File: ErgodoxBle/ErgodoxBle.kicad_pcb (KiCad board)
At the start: 2 copper layers, 182.8 x 158.9 mm, 120 parts, among them SW0:10 SW0:3, SW0:11 SW0:2, SW0:12 SW0:1, SW0:7 SW0:6, SW0:8 SW0:5, SW0:9 SW0:4, SW1:10 SW1:3, SW1:11 SW1:2, SW1:12 SW1:1, SW1:13 SW1:0, SW1:9 SW1:4, SW2:10 SW2:3, SW2:11 SW2:2, SW2:12 SW2:1, SW2:13 SW2:0, SW2:7 SW2:6, SW2:8 SW2:5, SW2:9 SW2:4, SW3:10 SW3:3, SW3:11 SW3:2, SW3:12 SW3:1, SW3:13 SW3:0, SW3:8 SW3:5, SW3:9 SW3:4, SW4:10 SW4:3, SW4:11 SW4:2, SW4:12 SW4:1, SW4:13 SW4:0, SW4:7 SW4:6, SW4:8 SW4:5, SW4:9 SW4:4, SW5:10 SW5:3, SW5:11 SW5:2, SW5:12 SW5:1, SW5:13 SW5:0, SW5:7 SW5:6, SW5:8 SW5:5, SW5:9 SW5:4

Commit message: schema and pcb pdf
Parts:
- removed the REF** at (172.9, 56.5)
- removed the REF** at (143.3, 76.1)
- removed the REF** at (67.8, 145.7)
- removed the REF** at (96.1, 157.6)
- removed the REF** at (158.3, 141.6)
- removed the REF** at (149.2, 145.2)
- removed the REF** at (142.6, 147.3)
- removed the REF** at (156.2, 126.8)
- removed the REF** at (154.9, 87.9)
- removed the REF** at (156.0, 105.3)
- removed the REF** at (156.3, 113.7)
- removed the REF** at (60.6, 176.1)
- removed the REF** at (91.8, 70.0)
- removed the REF** at (167.9, 110.0)
- removed the REF** at (138.9, 141.5)
- removed the REF** at (121.4, 84.8)
- removed the REF** at (121.4, 67.6)
- removed the REF** at (120.7, 124.0)
- removed the REF** at (123.4, 104.2)
- removed the REF** at (92.4, 88.5)
- removed the REF** at (103.5, 76.0)
- removed the REF** at (73.4, 164.6)
- removed the REF** at (177.3, 37.8)
- removed the REF** at (91.8, 108.3)
- removed the REF** at (168.9, 71.3)
- removed the REF** at (149.0, 49.6)
- removed the REF** at (139.6, 45.1)
- removed the REF** at (148.9, 68.7)
- added REF**: VIA-0.6mm, Keebio-Parts:VIA-0.6mm, F.Cu at (142.2, 38.5)
- added REF**: VIA-0.6mm, Keebio-Parts:VIA-0.6mm, F.Cu at (166.8, 129.4)
- added REF**: VIA-0.6mm, Keebio-Parts:VIA-0.6mm, F.Cu at (168.5, 109.1)
- added REF**: VIA-0.6mm, Keebio-Parts:VIA-0.6mm, F.Cu at (154.3, 86.6)
- added REF**: VIA-0.6mm, Keebio-Parts:VIA-0.6mm, F.Cu at (100.5, 123.8)
- added REF**: VIA-0.6mm, Keebio-Parts:VIA-0.6mm, F.Cu at (139.2, 122.6)
- added REF**: VIA-0.6mm, Keebio-Parts:VIA-0.6mm, F.Cu at (139.5, 104.1)
- added REF**: VIA-0.6mm, Keebio-Parts:VIA-0.6mm, F.Cu at (139.6, 90.9)
- added REF**: VIA-0.6mm, Keebio-Parts:VIA-0.6mm, F.Cu at (168.2, 71.8)
- added REF**: VIA-0.6mm, Keebio-Parts:VIA-0.6mm, F.Cu at (92.0, 69.1)
- added REF**: VIA-0.6mm, Keebio-Parts:VIA-0.6mm, F.Cu at (139.5, 65.7)
- added REF**: VIA-0.6mm, Keebio-Parts:VIA-0.6mm, F.Cu at (132.5, 38.3)
- added REF**: VIA-0.6mm, Keebio-Parts:VIA-0.6mm, F.Cu at (139.1, 136.7)
- added REF**: VIA-0.6mm, Keebio-Parts:VIA-0.6mm, F.Cu at (120.9, 137.0)
- added REF**: VIA-0.6mm, Keebio-Parts:VIA-0.6mm, F.Cu at (97.6, 136.9)
- added REF**: VIA-0.6mm, Keebio-Parts:VIA-0.6mm, F.Cu at (176.2, 38.4)
- added REF**: VIA-0.6mm, Keebio-Parts:VIA-0.6mm, F.Cu at (91.7, 89.2)
- added REF**: VIA-0.6mm, Keebio-Parts:VIA-0.6mm, F.Cu at (92.4, 108.4)
- added REF**: VIA-0.6mm, Keebio-Parts:VIA-0.6mm, F.Cu at (67.7, 146.4)
- added REF**: VIA-0.6mm, Keebio-Parts:VIA-0.6mm, F.Cu at (96.3, 158.8)
- added REF**: VIA-0.6mm, Keebio-Parts:VIA-0.6mm, F.Cu at (141.6, 148.2)
- added REF**: VIA-0.6mm, Keebio-Parts:VIA-0.6mm, F.Cu at (162.6, 137.2)
- added U_VR_IC1: AMS1117-3.3, Package_TO_SOT_SMD:SOT-223-3_TabPin2, B.Cu at (124.7, 43.1)
- J_Audio_B1, J_Audio_F1: footprint Connector_Audio:Jack_3.5mm_PJ320D_Horizontal -> Keebio-Parts:TRRS-PJ-320D
- moved J_Audio_F1 6.41 mm to (86.3, 30.5), turned to 180 degrees
- moved J_Audio_B1 6.40 mm to (86.3, 30.5), turned to 0 degrees
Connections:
- USB_C1 pad 11: /Vcc -> /VccR
- USB_C1 pad 2: /Vcc -> /VccR
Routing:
- net /VccR: track 0.00 -> 25.3 mm, vias 0 -> 2
- net GND: track 23.5 -> 8.96 mm
- net /Vcc: track 140.4 -> 132.7 mm, vias 3 -> 2
- net /CC2: track 6.39 -> 11.5 mm
- net /D-: track 71.0 -> 75.8 mm
- net /CC1: track 7.77 -> 12.5 mm
- net /D+: track 71.7 -> 73.9 mm, vias 0 -> 3
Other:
- net class Default: clearance 0.3048 -> 0.01778
- rule trace_clearance: 0.3048 -> 0.01778

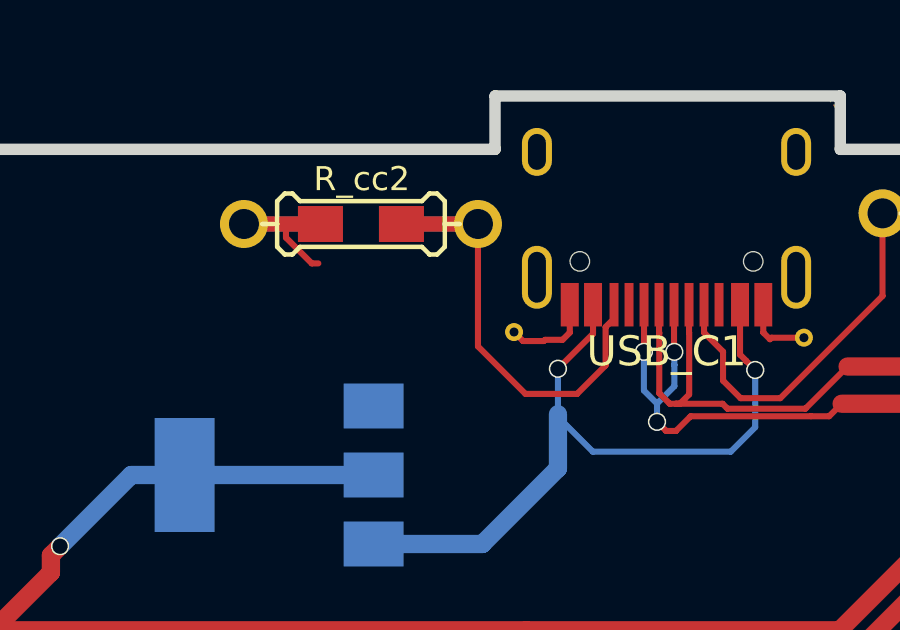
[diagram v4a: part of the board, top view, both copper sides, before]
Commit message: updated USB-C pad and added zone filled pdf
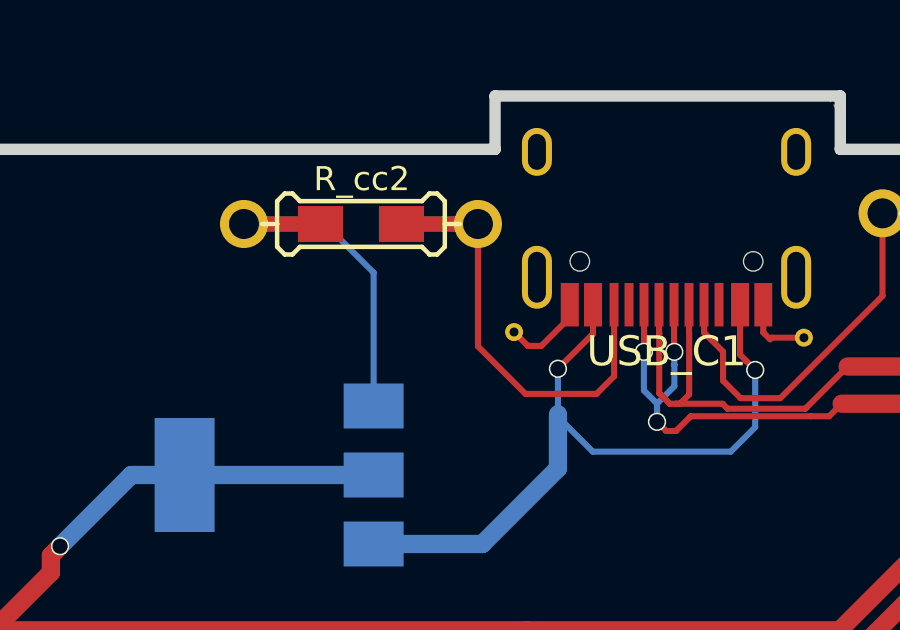
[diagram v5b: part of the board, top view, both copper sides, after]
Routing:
- net GND: track 8.96 -> 13.4 mm
- net /CC2: track 11.5 -> 12.4 mm
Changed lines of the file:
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@@
     (thickness 1.6002)
     (drawings 31)
-    (tracks 1051)
+    (tracks 1047)
     (zones 0)
     (modules 115)
@@
   (segment (start 140.8422 38.3666) (end 141.06398 38.58838) (width 0.2032) (layer Front) (net 54))
   (segment (start 140.8422 37.4384) (end 140.8422 38.3666) (width 0.2032) (layer Front) (net 54))
-  (segment (start 134.3922 38.3666) (end 134.1508 38.608) (width 0.2032) (layer Front) (net 54))
-  (segment (start 134.3922 37.4384) (end 134.3922 38.3666) (width 0.2032) (layer Front) (net 54))
-  (segment (start 134.1508 38.608) (end 133.5659 38.608) (width 0.2032) (layer Front) (net 54))
-  (segment (start 124.9318 35.2004) (end 125.79178 36.06038) (width 0.2032) (layer Front) (net 54))
-  (segment (start 124.9318 34.7472) (end 124.9318 35.2004) (width 0.2032) (layer Front) (net 54))
-  (segment (start 125.79178 36.06038) (end 126.01194 36.06038) (width 0.2032) (layer Front) (net 54))
   (segment (start 151.217 34.8448) (end 151.49322 35.12102) (width 0.2032) (layer Front) (net 54))
   (segment (start 151.217 34.3916) (end 151.217 34.8448) (width 0.2032) (layer Front) (net 54))
   (segment (start 151.49322 35.12102) (end 151.49322 35.50412) (width 0.2032) (layer Front) (net 54))
-  (segment (start 133.524981 38.648919) (end 133.5659 38.608) (width 0.2032) (layer Front) (net 54))
-  (segment (start 132.834659 38.648919) (end 133.524981 38.648919) (width 0.2032) (layer Front) (net 54))
-  (segment (start 132.53466 38.34892) (end 132.834659 38.648919) (width 0.2032) (layer Front) (net 54))
   (segment (start 141.11548 38.53688) (end 142.19682 38.53688) (width 0.2032) (layer Front) (net 54))
   (segment (start 141.06398 38.58838) (end 141.11548 38.53688) (width 0.2032) (layer Front) (net 54))
+  (segment (start 126.2318 34.7472) (end 126.0818 34.7472) (width 0.2032) (layer Back) (net 54))
+  (segment (start 127.85384 36.36924) (end 126.2318 34.7472) (width 0.2032) (layer Back) (net 54))
+  (segment (start 127.85384 40.81396) (end 127.85384 36.36924) (width 0.2032) (layer Back) (net 54))
+  (segment (start 134.3922 37.8634) (end 133.4444 38.8112) (width 0.2032) (layer Front) (net 54))
+  (segment (start 132.99694 38.8112) (end 132.53466 38.34892) (width 0.2032) (layer Front) (net 54))
+  (segment (start 133.4444 38.8112) (end 132.99694 38.8112) (width 0.2032) (layer Front) (net 54))
   (segment (start 99.1686 37.8606) (end 97.9932 39.036) (width 0.6) (layer Back) (net 55))
   (segment (start 102.489 37.8606) (end 99.1686 37.8606) (width 0.6) (layer Back) (net 55))
@@
   (segment (start 187.1472 39.497) (end 143.65224 39.497) (width 0.6096) (layer Front) (net 58))
   (segment (start 193.6242 39.4716) (end 193.6242 39.497) (width 0.6096) (layer Front) (net 58))
-  (segment (start 135.586581 38.182439) (end 135.586581 39.460059) (width 0.2032) (layer Front) (net 59))
   (segment (start 135.8672 37.4384) (end 135.8672 37.90182) (width 0.2032) (layer Front) (net 59))
-  (segment (start 135.8672 37.90182) (end 135.586581 38.182439) (width 0.2032) (layer Front) (net 59))
-  (segment (start 135.586581 39.460059) (end 134.63524 40.4114) (width 0.2032) (layer Front) (net 59))
-  (segment (start 134.63524 40.4114) (end 132.91566 40.4114) (width 0.2032) (layer Front) (net 59))
-  (segment (start 131.3318 38.82754) (end 131.3318 34.7472) (width 0.2032) (layer Front) (net 59))
-  (segment (start 132.91566 40.4114) (end 131.3318 38.82754) (width 0.2032) (layer Front) (net 59))
+  (segment (start 135.8672 39.82714) (end 135.8672 37.4384) (width 0.2032) (layer Front) (net 59))
+  (segment (start 135.28294 40.4114) (end 135.8672 39.82714) (width 0.2032) (layer Front) (net 59))
+  (segment (start 132.91566 40.4114) (end 135.28294 40.4114) (width 0.2032) (layer Front) (net 59))
+  (segment (start 131.3318 34.7472) (end 131.3318 38.82754) (width 0.2032) (layer Front) (net 59))
+  (segment (start 131.3318 38.82754) (end 132.91566 40.4114) (width 0.2032) (layer Front) (net 59))
   (via (at 86.0552 36.6522) (size 0.6096) (drill 0.508) (layers Front Back) (net 60))
   (segment (start 83.0338 36.7058) (end 86.0016 36.7058) (width 0.6) (layer Back) (net 60))
@@
     (connect_pads (clearance 0.508))
     (min_thickness 0.254)
-    (fill (arc_segments 16) (thermal_gap 0.508) (thermal_bridge_width 0.508))
+    (fill yes (arc_segments 16) (thermal_gap 0.508) (thermal_bridge_width 0.508))
     (polygon
       (pts
@@
     (connect_pads (clearance 0.508))
     (min_thickness 0.254)
-    (fill (arc_segments 16) (thermal_gap 0.508) (thermal_bridge_width 0.508))
+    (fill yes (arc_segments 16) (thermal_gap 0.508) (thermal_bridge_width 0.508))
     (polygon
       (pts
